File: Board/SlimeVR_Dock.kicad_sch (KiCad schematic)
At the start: 36 parts, among them J1 USB_C_Receptacle_USB2.0_16P, J10_ToR0 Conn_01x02_Pin, J10_ToR1 Conn_01x02_Pin, J12_FromR0 Conn_01x02_Pin, J12_FromR1 Conn_01x02_Pin, J2 USB_C_Receptacle_USB2.0_16P, J3 USB_C_Receptacle_USB2.0_16P, J4 USB_C_Receptacle_USB2.0_16P, J5 USB_C_Receptacle_USB2.0_16P, J6 USB_C_Receptacle_USB2.0_16P, J7 USB_C_Receptacle_USB2.0_16P, J8 USB_C_Receptacle_USB2.0_16P, J9_Main USB_C_Receptacle_USB2.0_16P, M1 NF-A4x10 24V PWM, Q1 AO3401A, U1 ESP32-C3-WROOM-02, U10 INA226, U11 INA226, U12 INA226, U13 AP22652W6-7, U14 AP22652W6-7, U15 XC6220B331MR, U16 DS18B20, U2 CH224K, U3 AP22652W6-7, U4 AP22652W6-7, U5 INA226, U6 INA226, U7 INA226, U8 INA226, U9 INA226

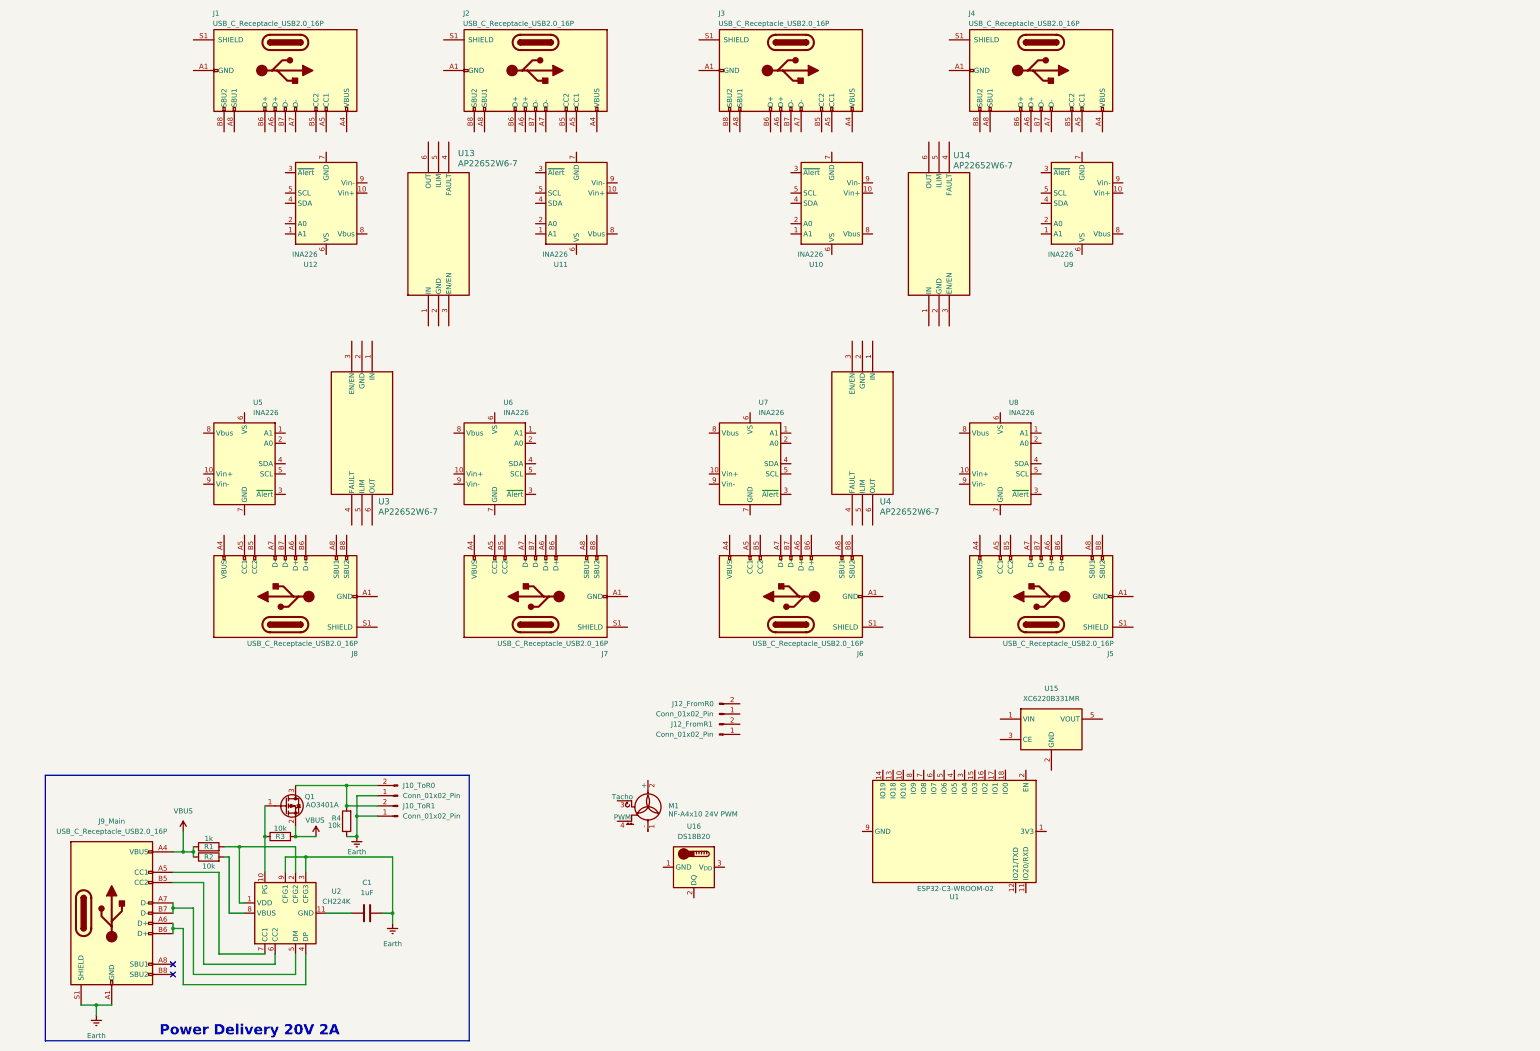
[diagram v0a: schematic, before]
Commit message: made subschema for usb-c
subschea for USB-Cs for more comact schema
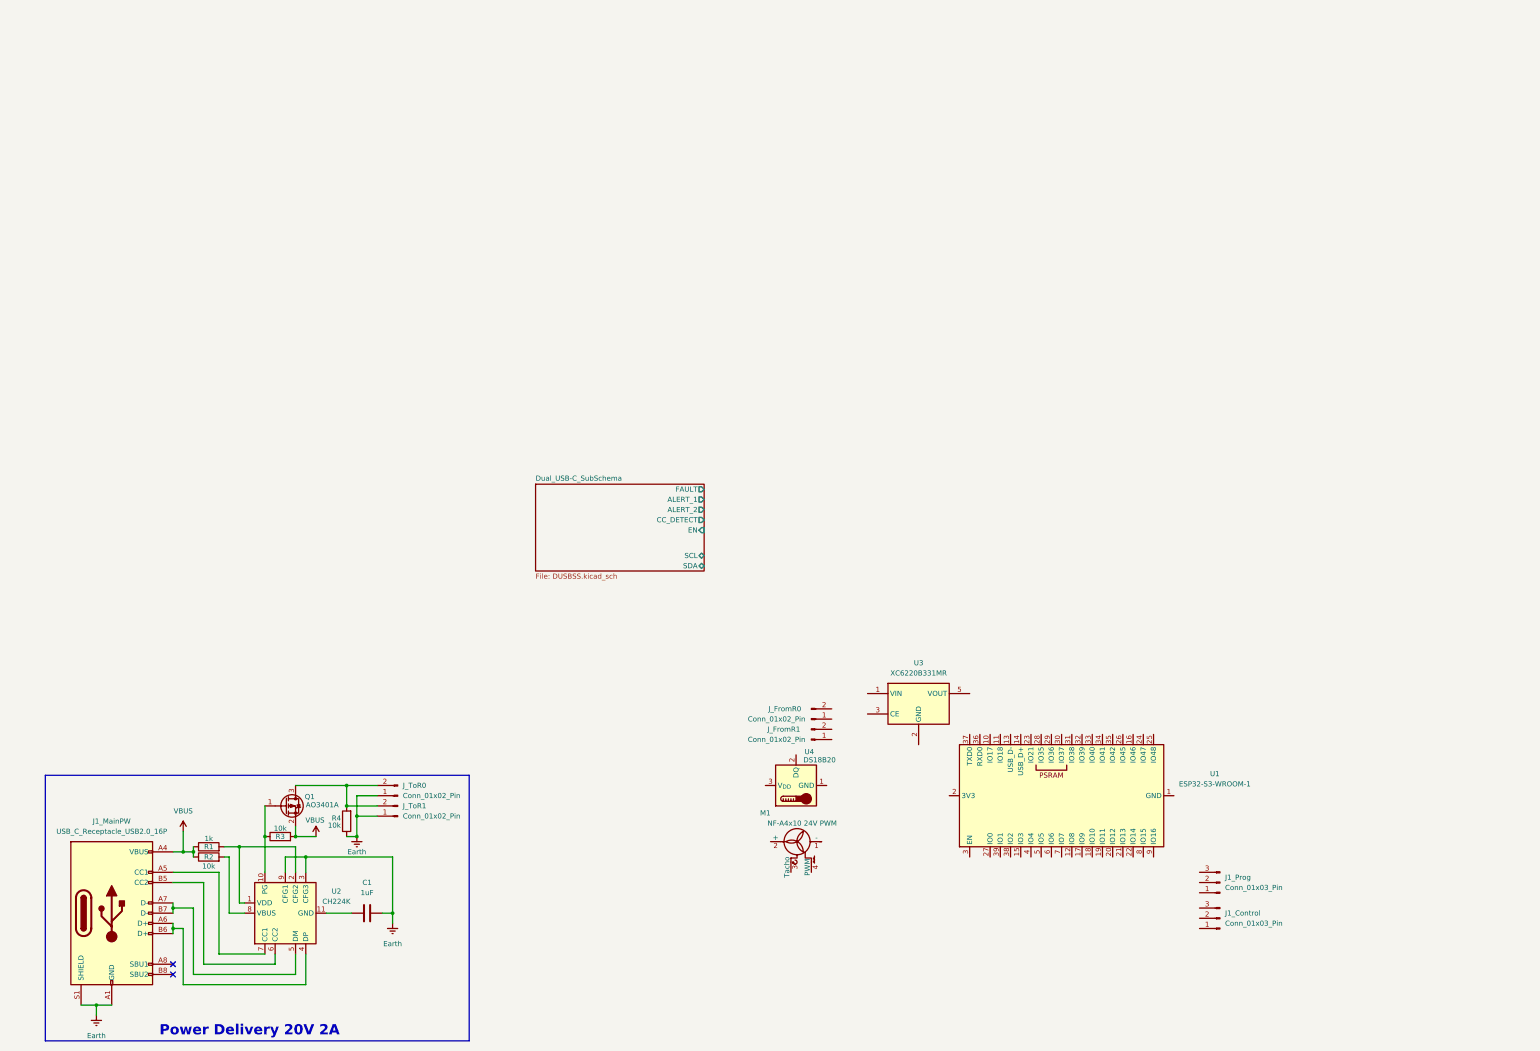
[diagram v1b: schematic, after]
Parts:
- removed J1, J2, J3, J4, J5, J6, J7, J8: USB_C_Receptacle_USB2.0_16P, symbol Connector:USB_C_Receptacle_USB2.0_16P
- removed U1: ESP32-C3-WROOM-02, RF_Module:ESP32-C3-WROOM-02, symbol RF_Module:ESP32-C3-WROOM-02
- removed U10, U11, U12, U5, U6, U7, U8, U9: INA226, Package_SO:VSSOP-10_3x3mm_P0.5mm, symbol Sensor_Energy:INA226
- removed U13, U14, U3, U4: AP22652W6-7, SOIC_52W6-7_DIO, symbol Library:AP22652W6-7
- added J1_Control, J1_Prog: Conn_01x03_Pin, symbol Connector:Conn_01x03_Pin
- added U1: ESP32-S3-WROOM-1, RF_Module:ESP32-S3-WROOM-1, symbol RF_Module:ESP32-S3-WROOM-1
- renumbered J9_Main to J1_MainPW, J12_FromR0 to J_FromR0, J12_FromR1 to J_FromR1, J10_ToR0 to J_ToR0, J10_ToR1 to J_ToR1, U15 to U3, U16 to U4
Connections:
- new net: U1.1 (GND), U1.40 (GND), U1.41 (GND)
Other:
- added sheet Dual_USB-C_SubSchema (DUSBSS.kicad_sch)
- moved on the sheet: J_FromR0, J_FromR1, M1, U3, U4

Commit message: New Layout and power
Made power for 3v3
all usb added
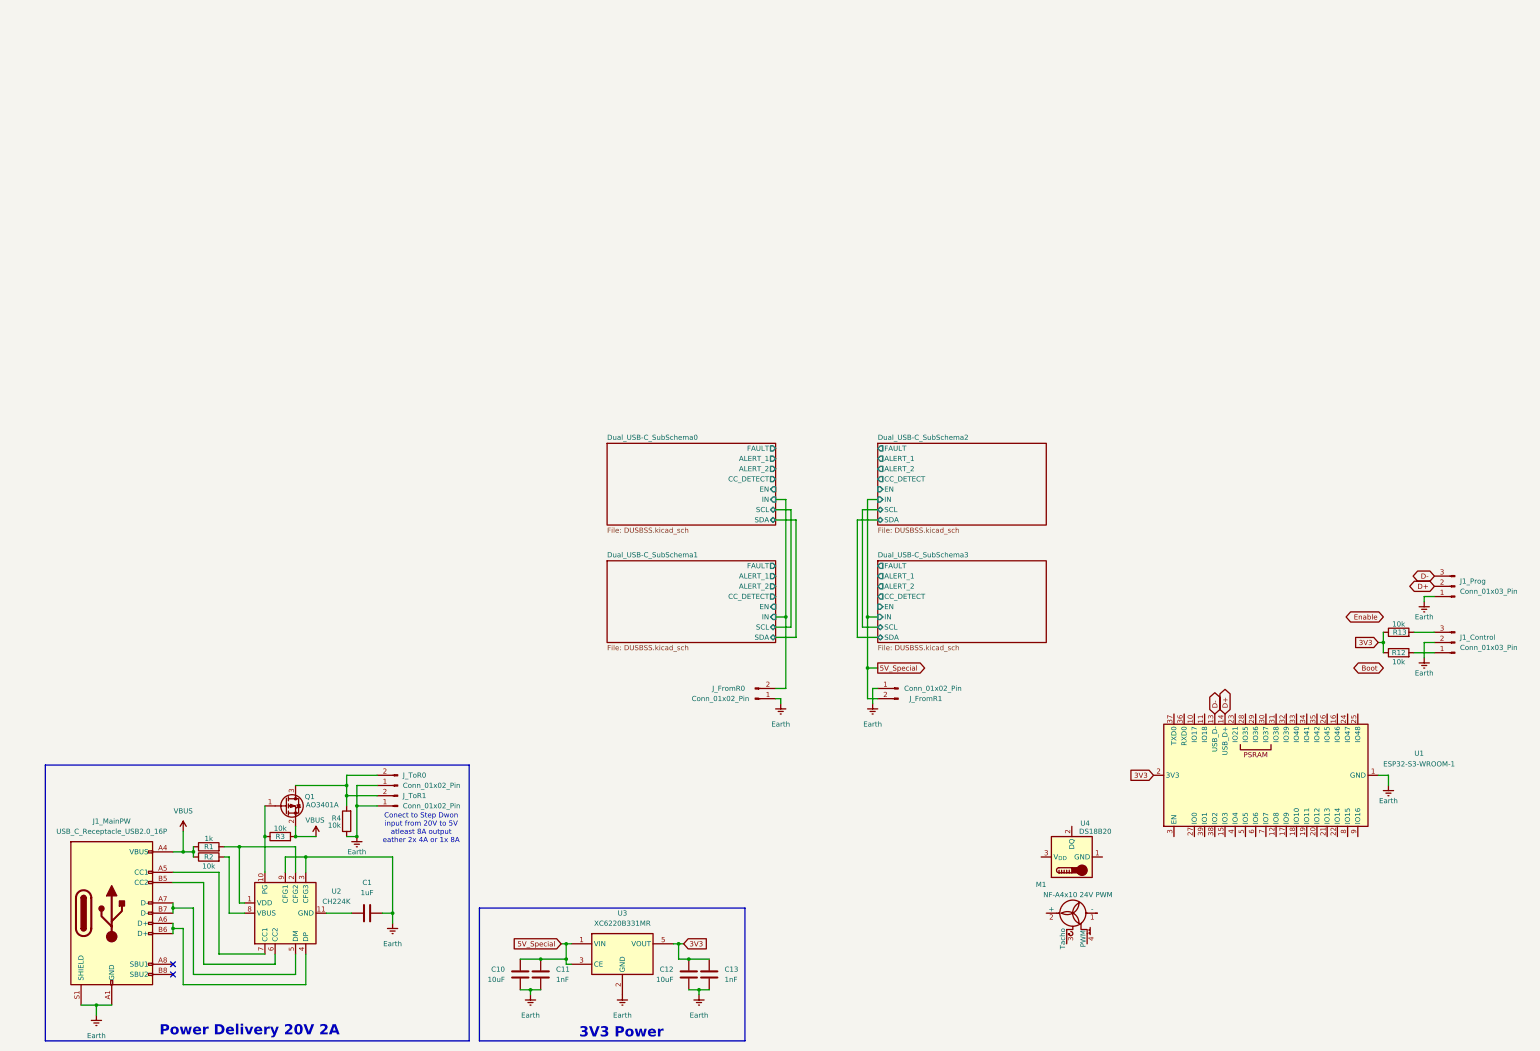
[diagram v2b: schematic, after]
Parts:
- added C10, C12: 10uF, symbol Device:C
- added C11, C13: 1nF, symbol Device:C
- added R12, R13: 10k, symbol Device:R
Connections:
- net Earth: now also J1_Control.2 (Pin_2), J1_Prog.1 (Pin_1), J_FromR0.1 (Pin_1), J_FromR1.1 (Pin_1), U1.1 (GND), U1.40 (GND), U1.41 (GND), U3.2 (GND), C10.2, C11.2, C12.2, C13.2
- net 5V_Special: now reaches J_FromR1.2 (Pin_2)
- net 5V_Special: now also U3.1 (VIN), U3.3 (CE), C10.1, C11.1
- net D-: now reaches U1.13 (USB_D-)
- net D-: now also J1_Prog.3 (Pin_3)
- net D+: now reaches U1.14 (USB_D+)
- net D+: now also J1_Prog.2 (Pin_2)
- net 3V3: now reaches U1.2 (3V3)
- net 3V3: now also U3.5 (VOUT), C12.1, C13.1, R12.1, R13.1
- net Dual_USB-C_SubSchema0/IN: now reaches J_FromR0.2 (Pin_2)
- net at J1_Control.1 (Pin_1): now also R12.2
- net at J1_Control.3 (Pin_3): now also R13.2
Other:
- sheet Dual_USB-C_SubSchema renamed Dual_USB-C_SubSchema0
- added sheet Dual_USB-C_SubSchema1 (DUSBSS.kicad_sch)
- added sheet Dual_USB-C_SubSchema2 (DUSBSS.kicad_sch)
- added sheet Dual_USB-C_SubSchema3 (DUSBSS.kicad_sch)
- sheet Dual_USB-C_SubSchema0 ports: added IN; removed none
- note added: "3V3 Power"
- note added: "Conect to Step Dwon input from 20V to 5V atleast 8A output eather 2x 4A or 1x 8A"
- moved on the sheet: J1_Control, J1_Prog, J_FromR0, J_FromR1, J_ToR0, J_ToR1, M1, U1, U3, U4

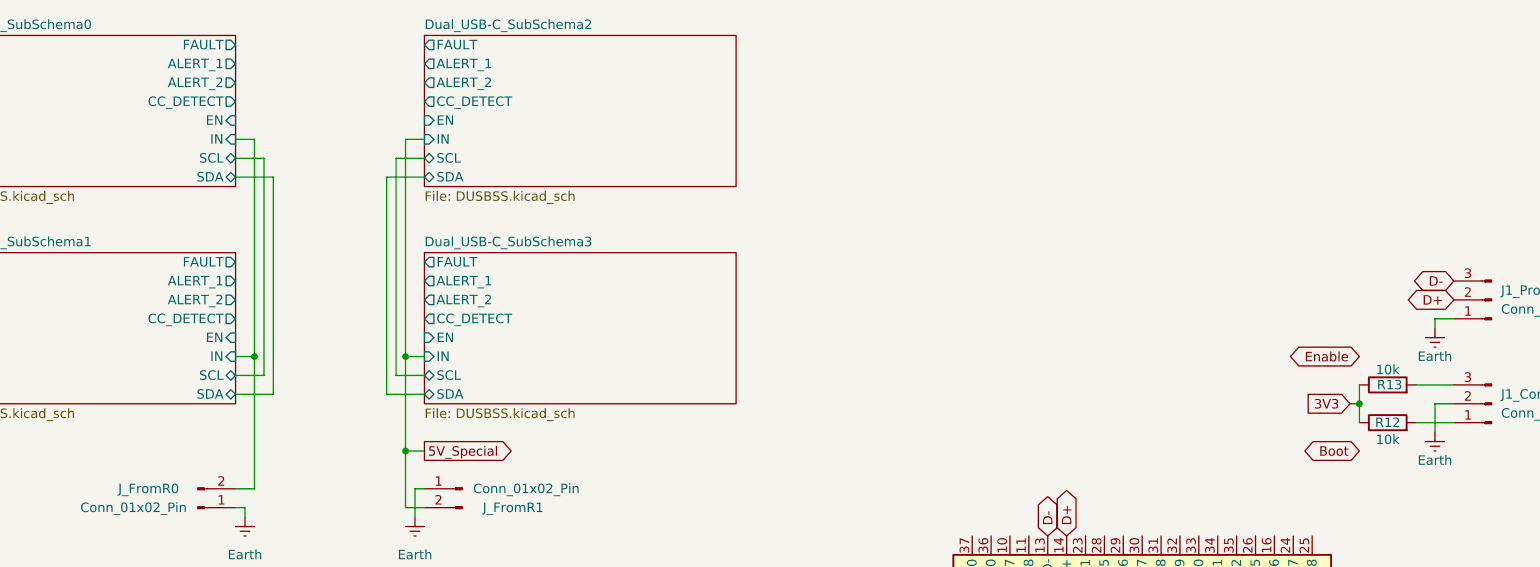
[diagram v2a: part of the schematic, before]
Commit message: Saving pins
-4 pins to connect to gpio thanks for ability to use two or more alert pins on one gpio
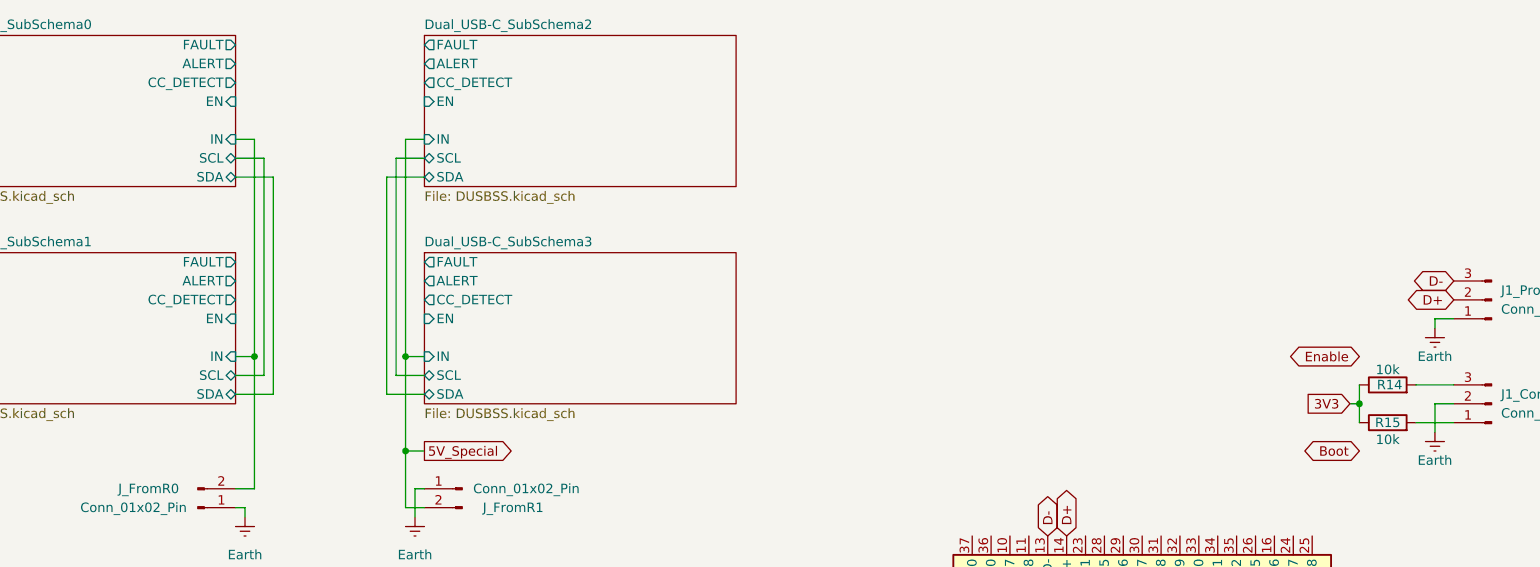
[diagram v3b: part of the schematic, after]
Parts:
- renumbered R13 to R14, R12 to R15
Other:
- sheet Dual_USB-C_SubSchema0 ports: added ALERT; removed ALERT_1, ALERT_2
- sheet Dual_USB-C_SubSchema1 ports: added ALERT; removed ALERT_1, ALERT_2
- sheet Dual_USB-C_SubSchema2 ports: added ALERT; removed ALERT_1, ALERT_2
- sheet Dual_USB-C_SubSchema3 ports: added ALERT; removed ALERT_1, ALERT_2
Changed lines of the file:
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@@
 		(on_board yes)
 		(dnp no)
-		(property "Reference" "R12"
+		(property "Reference" "R15"
 			(at 364.49 173.99 90)
 			(effects
@@
 			(project ""
 				(path "/06ff9557-1f9b-4670-8a34-bb7684a016dd"
-					(reference "R12")
+					(reference "R15")
 					(unit 1)
 				)
@@
 		(on_board yes)
 		(dnp no)
-		(property "Reference" "R13"
+		(property "Reference" "R14"
 			(at 364.744 168.91 90)
 			(effects
@@
 			(project "SlimeVR_Dock"
 				(path "/06ff9557-1f9b-4670-8a34-bb7684a016dd"
-					(reference "R13")
+					(reference "R14")
 					(unit 1)
 				)
@@
 			)
 		)
-		(pin "ALERT_1" output
-			(at 209.55 125.73 0)
+		(pin "EN" input
+			(at 209.55 130.81 0)
 			(effects
 				(font
@@
 			)
 		)
-		(pin "ALERT_2" output
+		(pin "CC_DETECT" output
 			(at 209.55 128.27 0)
-			(effects
-				(font
-					(size 1.27 1.27)
-				)
-				(justify right)
-			)
-		)
-		(pin "EN" input
-			(at 209.55 133.35 0)
-			(effects
-				(font
-					(size 1.27 1.27)
-				)
-				(justify right)
-			)
-		)
-		(pin "CC_DETECT" output
-			(at 209.55 130.81 0)
 			(effects
 				(font
@@
 		(pin "IN" input
 			(at 209.55 135.89 0)
+			(effects
+				(font
+					(size 1.27 1.27)
+				)
+				(justify right)
+			)
+		)
+		(pin "ALERT" output
+			(at 209.55 125.73 0)
 			(effects
 				(font
@@
 			)
 		)
-		(pin "ALERT_1" output
-			(at 234.95 125.73 180)
+		(pin "EN" input
+			(at 234.95 130.81 180)
 			(effects
 				(font
@@
 			)
 		)
-		(pin "ALERT_2" output
+		(pin "CC_DETECT" output
 			(at 234.95 128.27 180)
-			(effects
-				(font
-					(size 1.27 1.27)
-				)
-				(justify left)
-			)
-		)
-		(pin "EN" input
-			(at 234.95 133.35 180)
-			(effects
-				(font
-					(size 1.27 1.27)
-				)
-				(justify left)
-			)
-		)
-		(pin "CC_DETECT" output
-			(at 234.95 130.81 180)
 			(effects
 				(font
@@
 		(pin "IN" input
 			(at 234.95 135.89 180)
+			(effects
+				(font
+					(size 1.27 1.27)
+				)
+				(justify left)
+			)
+		)
+		(pin "ALERT" output
+			(at 234.95 125.73 180)
 			(effects
 				(font
@@
 			)
 		)
-		(pin "ALERT_1" output
-			(at 234.95 154.94 180)
+		(pin "EN" input
+			(at 234.95 160.02 180)
 			(effects
 				(font
@@
 			)
 		)
-		(pin "ALERT_2" output
+		(pin "CC_DETECT" output
 			(at 234.95 157.48 180)
-			(effects
-				(font
-					(size 1.27 1.27)
-				)
-				(justify left)
-			)
-		)
-		(pin "EN" input
-			(at 234.95 162.56 180)
-			(effects
-				(font
-					(size 1.27 1.27)
-				)
-				(justify left)
-			)
-		)
-		(pin "CC_DETECT" output
-			(at 234.95 160.02 180)
 			(effects
 				(font
@@
 		(pin "IN" input
 			(at 234.95 165.1 180)
+			(effects
+				(font
+					(size 1.27 1.27)
+				)
+				(justify left)
+			)
+		)
+		(pin "ALERT" output
+			(at 234.95 154.94 180)
 			(effects
 				(font
@@
 			)
 		)
-		(pin "ALERT_1" output
-			(at 209.55 154.94 0)
+		(pin "EN" input
+			(at 209.55 160.02 0)
 			(effects
 				(font
@@
 			)
 		)
-		(pin "ALERT_2" output
+		(pin "CC_DETECT" output
 			(at 209.55 157.48 0)
-			(effects
-				(font
-					(size 1.27 1.27)
-				)
-				(justify right)
-			)
-		)
-		(pin "EN" input
-			(at 209.55 162.56 0)
-			(effects
-				(font
-					(size 1.27 1.27)
-				)
-				(justify right)
-			)
-		)
-		(pin "CC_DETECT" output
-			(at 209.55 160.02 0)
 			(effects
 				(font
@@
 			(effects
 				(font
+					(size 1.27 1.27)
+				)
+				(justify right)
+			)
+		)
+		(pin "ALERT" output
+			(at 209.55 154.94 0)
+			(effects
+				(font
